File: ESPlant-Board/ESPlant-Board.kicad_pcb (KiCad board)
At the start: 2 copper layers, 22 x 127 mm, 35 parts, among them J1 Conn_01x05, U13 ESP32-C6-MINI-1/U, U3 Reset, U4 Boot, U5 Temp/Humid-Sensor, U6 Light sensor, U7 AMS1117-3_3, U8 MK-12C02-G025

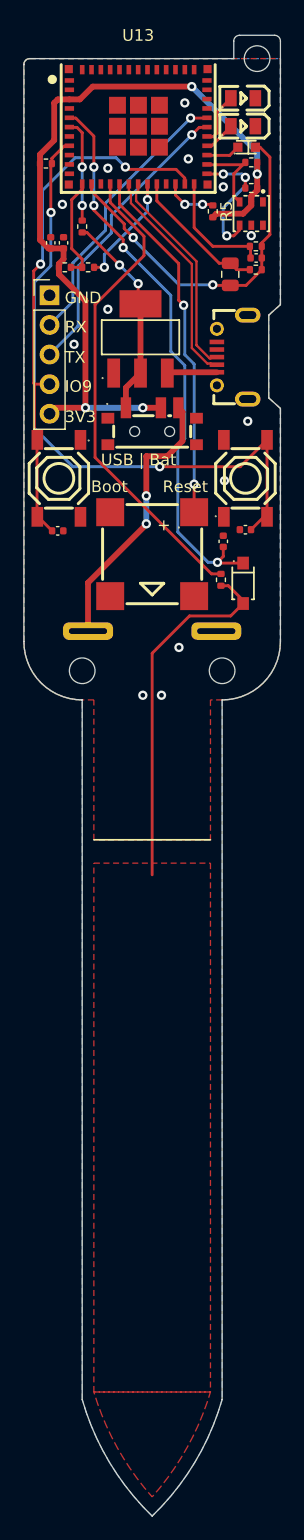
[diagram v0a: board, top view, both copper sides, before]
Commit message: Board: Replace Micro USB with USB type c
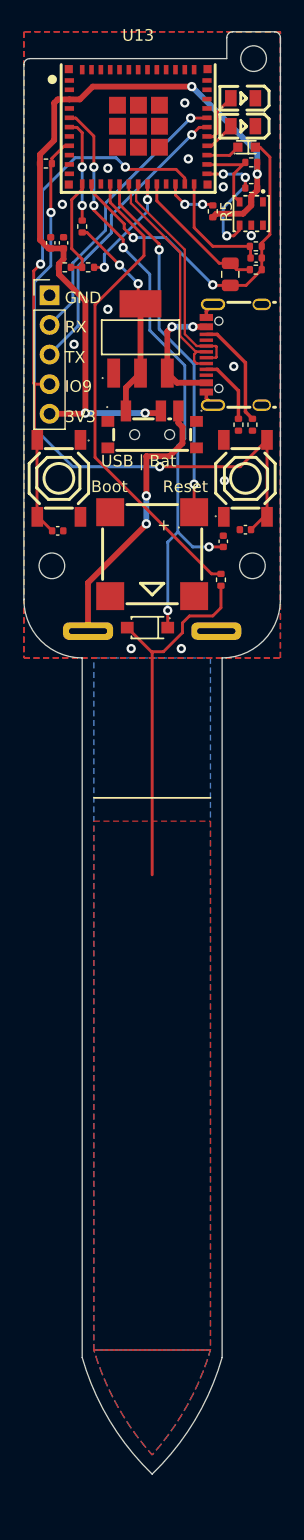
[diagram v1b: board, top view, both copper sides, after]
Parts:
- removed USB1: micro_USBFemale, CustomFootprints:MICRO-USB-SMD_5P-P0.65-H-F_C10418
- added R11: 5k1, Resistor_SMD:R_0402_1005Metric, F.Cu at (118.4, 131.4)
- added R12: 5k1, Resistor_SMD:R_0402_1005Metric, F.Cu at (119.6, 131.4)
- added U1: HC-TYPE-C-16P-01A-G, CustomFootprints:USB-C-SMD_G-SWITCH_GT-USB-7010EN, F.Cu at (118.0, 125.4)
- moved D2 9.04 mm to (110.6, 148.8), turned to 180 degrees
- moved U10 2.10 mm to (99.5, 143.5)
- moved U2 2.10 mm to (122.4, 143.5)
- moved U8 0.27 mm to (111.0, 131.8)
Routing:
- net Net-(U1-CC2): track 0.00 -> 9.42 mm
- net Net-(U7-VIN): track 4.28 -> 10.9 mm, vias 0 -> 2
- net Net-(U1-CC1): track 0.00 -> 5.92 mm
- net /AD_Capacitance: track 48.4 -> 53.2 mm, vias 4 -> 5
- net GND: track 0.04 -> 2.75 mm, vias 13 -> 12
- net /D-: track 19.0 -> 20.5 mm
- net /D+: track 18.3 -> 19.6 mm
- net /SensorCapV: track 31.4 -> 32.0 mm
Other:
- board size 22 x 127 mm -> 22 x 123.7 mm

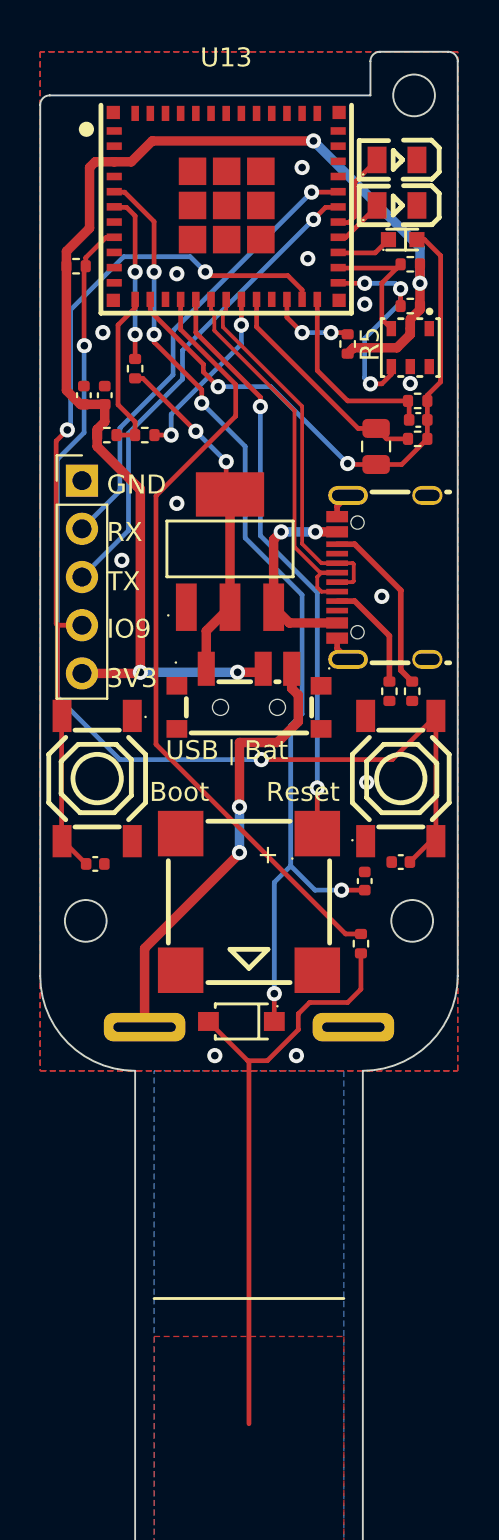
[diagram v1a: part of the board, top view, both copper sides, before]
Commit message: Board: Make board smaller
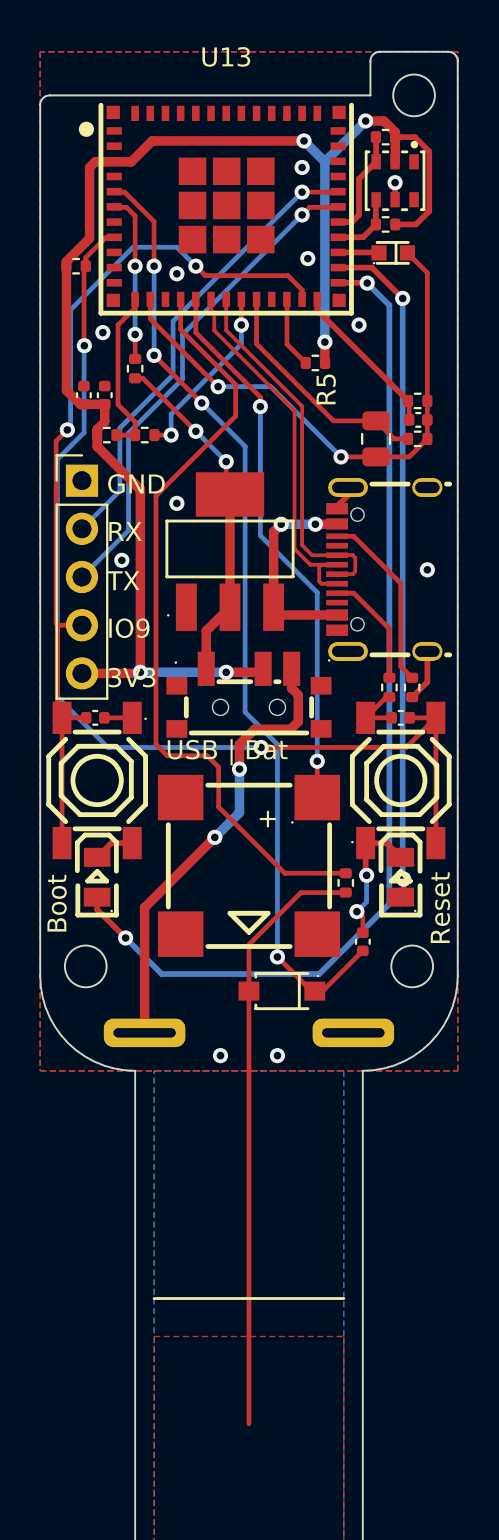
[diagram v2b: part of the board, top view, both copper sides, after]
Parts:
- moved D1 41.0 mm to (103.0, 141.2), turned to -90 degrees
- moved D3 35.4 mm to (119.0, 141.2), turned to -90 degrees
- moved U5 8.83 mm to (118.7, 104.5)
- moved C2 7.70 mm to (102.9, 132.8)
- moved C1 7.60 mm to (119.0, 132.8)
- moved R2 6.82 mm to (118.2, 102.2)
- moved R10 4.49 mm to (118.2, 106.8)
- moved R8 3.30 mm to (116.1, 141.5)
- moved C3 3.20 mm to (117.0, 144.6)
- moved D2 2.67 mm to (112.7, 147.2)
- moved R5 1.97 mm to (114.5, 114.1), turned to 0 degrees
- moved BZ1 1.90 mm to (111.0, 140.6)
- moved U6 0.86 mm to (118.6, 108.3)
- moved U1 0.42 mm to (118.0, 125.0)
- moved C7 0.40 mm to (117.7, 118.1)
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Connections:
- U13 pad 25: /TH_SDA -> /LED_GREEN
- U13 pad 26: /TH_SCL -> /LED_RED
- U13 pad 28: /LED_RED -> /TH_SDA
- U13 pad 29: /LED_GREEN -> /TH_SCL
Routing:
- net /LED_GREEN: track 4.47 -> 53.7 mm, vias 0 -> 2
- net /LED_RED: track 2.78 -> 35.7 mm, vias 0 -> 2
- net GND: track 2.75 -> 18.6 mm, vias 12 -> 13
- net /TH_SDA: track 12.0 -> 3.57 mm, vias 3 -> 0
- net +3V3: track 69.3 -> 77.3 mm, vias 4 -> 5
- net /AD_Capacitance: track 53.2 -> 50.3 mm, vias 5 -> 4
- net /Buzzer: track 30.8 -> 28.9 mm
- net /Light_Sensor_Select_1: track 10.2 -> 8.35 mm
- net /TH_SCL: track 7.38 -> 5.73 mm
- net /Light_Sensor_Analog: track 30.9 -> 29.2 mm
- net /Square_Wave_Signal: track 41.3 -> 40.4 mm
- net /EN: track 56.3 -> 55.4 mm
- net /Light_Sensor_In: track 2.94 -> 2.16 mm
- net /IO8: track 4.47 -> 3.71 mm, vias 2 -> 0
- net /Light_Sensor_Select_2: track 11.8 -> 12.4 mm
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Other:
- outline, holes or cut-outs redrawn

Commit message: Board: Add version number 2.1
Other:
- board text added: "ESPlant-v2.1"
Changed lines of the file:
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@@
     (effects (font (size 1 1) (thickness 0.15)) (justify left bottom mirror))
   )
-  (gr_text "M2" (at 121 102.5) (layer "B.SilkS")
+  (gr_text "M2" (at 120.9 102.8) (layer "B.SilkS")
     (effects (font (size 1 1) (thickness 0.15)) (justify left bottom mirror))
   )
@@
     (effects (font (size 1 1) (thickness 0.15)) (justify left bottom mirror))
   )
-  (gr_text "M2" (at 120.8 143.2) (layer "B.SilkS")
+  (gr_text "M2" (at 120.8 144.6) (layer "B.SilkS")
+    (effects (font (size 1 1) (thickness 0.15)) (justify left bottom mirror))
+  )
+  (gr_text "ESPlant-v2.1" (at 110.9 102.1) (layer "B.SilkS")
     (effects (font (size 1 1) (thickness 0.15)) (justify left bottom mirror))
   )
@@
     (effects (font (size 1 1) (thickness 0.15)) (justify left bottom mirror))
   )
-  (gr_text "M2" (at 103.6 143.2) (layer "B.SilkS")
+  (gr_text "M2" (at 103.6 144.6) (layer "B.SilkS")
     (effects (font (size 1 1) (thickness 0.15)) (justify left bottom mirror))
   )

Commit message: Board: Change from aht21 to aht21, fix kikit, produce board
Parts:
- U10, U11, U12, U2: footprint PCM_kikit:Tab_5mm -> CustomFootprints:MouseBites5mm
- moved U10 0.71 mm to (100.0, 143.0)
- moved U2 0.64 mm to (122.0, 143.0)
- moved U11 0.40 mm to (122.0, 104.0)
- moved U12 0.40 mm to (100.0, 104.0)
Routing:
- net GND: track 18.6 -> 19.9 mm, vias 13 -> 12
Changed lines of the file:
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@@
     )
   )
-  (footprint "PCM_kikit:Tab_5mm" (layer "F.Cu")
-    (at 122.45 104 180)
-    (descr "A symbol representing annotation for tab placement")
+  (footprint "CustomFootprints:MouseBites5mm" (layer "F.Cu")
+    (at 122.05 104 180)
     (property "Sheetfile" "ESPlant-Board.kicad_sch")
     (property "Sheetname" "")
     (property "dnp" "")
     (property "exclude_from_bom" "")
-    (attr exclude_from_pos_files exclude_from_bom)
-    (fp_text reference "U11" (at 0 -2) (layer "F.SilkS") hide
-        (effects (font (size 1 1) (thickness 0.15)))
-    )
-    (fp_text value "~" (at -2.75 -1) (layer "Dwgs.User")
-        (effects (font (size 1.2 1.2) (thickness 0.2)))
-    )
-    (fp_text user "KIKIT: width: 5mm" (at -5.5 0 90) (layer "Dwgs.User")
-        (effects (font (size 1 1) (thickness 0.15)))
-    )
-    (fp_line (start 0.25 0) (end -2.75 0)
+    (attr smd exclude_from_bom)
+    (fp_text reference "U11" (at 0 -0.5 180 unlocked) (layer "F.SilkS") hide
+        (effects (font (size 1 1) (thickness 0.1)))
+    )
+    (fp_text value "~" (at 0 1 180 unlocked) (layer "F.Fab")
+        (effects (font (size 1 1) (thickness 0.15)))
+    )
+    (fp_text user "KIKIT: width: 5mm" (at -6.004 -0.04 270) (layer "Dwgs.User")
+        (effects (font (size 1 1) (thickness 0.15)))
+    )
+    (fp_text user "${REFERENCE}" (at 0 2.5 180 unlocked) (layer "F.Fab")
+        (effects (font (size 1 1) (thickness 0.15)))
+    )
+    (fp_line (start -0.254 -0.04) (end -3.254 -0.04)
       (stroke (width 0.3) (type solid)) (layer "Dwgs.User"))
-    (fp_line (start 0.25 0) (end -0.75 -1)
+    (fp_line (start -0.254 -0.04) (end -1.254 -1.04)
       (stroke (width 0.3) (type solid)) (layer "Dwgs.User"))
-    (fp_line (start 0.25 0) (end -0.75 1)
+    (fp_line (start -0.254 -0.04) (end -1.254 0.96)
       (stroke (width 0.3) (type solid)) (layer "Dwgs.User"))
-    (fp_line (start 0.25 2.5) (end 0.25 -2.5)
+    (fp_line (start -0.254 2.46) (end -0.254 -2.54)
       (stroke (width 0.3) (type solid)) (layer "Dwgs.User"))
   )
-  (footprint "PCM_kikit:Tab_5mm" (layer "F.Cu")
-    (at 99.6 104)
-    (descr "A symbol representing annotation for tab placement")
+  (footprint "CustomFootprints:MouseBites5mm" (layer "F.Cu")
+    (at 100 104)
     (property "Sheetfile" "ESPlant-Board.kicad_sch")
     (property "Sheetname" "")
     (property "dnp" "")
     (property "exclude_from_bom" "")
-    (attr exclude_from_pos_files exclude_from_bom)
-    (fp_text reference "U12" (at 0 -2) (layer "F.SilkS") hide
-        (effects (font (size 1 1) (thickness 0.15)))
-    )
-    (fp_text value "~" (at -2.75 -1) (layer "Dwgs.User")
-        (effects (font (size 1.2 1.2) (thickness 0.2)))
-    )
-    (fp_text user "KIKIT: width: 5mm" (at -5.5 0 90) (layer "Dwgs.User")
-        (effects (font (size 1 1) (thickness 0.15)))
-    )
-    (fp_line (start 0.25 0) (end -2.75 0)
+    (attr smd exclude_from_bom)
+    (fp_text reference "U12" (at 0 -0.5 unlocked) (layer "F.SilkS") hide
+        (effects (font (size 1 1) (thickness 0.1)))
+    )
+    (fp_text value "~" (at 0 1 unlocked) (layer "F.Fab")
+        (effects (font (size 1 1) (thickness 0.15)))
+    )
+    (fp_text user "KIKIT: width: 5mm" (at -6.004 -0.04 90) (layer "Dwgs.User")
+        (effects (font (size 1 1) (thickness 0.15)))
+    )
+    (fp_text user "${REFERENCE}" (at 0 2.5 unlocked) (layer "F.Fab")
+        (effects (font (size 1 1) (thickness 0.15)))
+    )
+    (fp_line (start -0.254 -0.04) (end -3.254 -0.04)
       (stroke (width 0.3) (type solid)) (layer "Dwgs.User"))
-    (fp_line (start 0.25 0) (end -0.75 -1)
+    (fp_line (start -0.254 -0.04) (end -1.254 -1.04)
       (stroke (width 0.3) (type solid)) (layer "Dwgs.User"))
-    (fp_line (start 0.25 0) (end -0.75 1)
+    (fp_line (start -0.254 -0.04) (end -1.254 0.96)
       (stroke (width 0.3) (type solid)) (layer "Dwgs.User"))
-    (fp_line (start 0.25 2.5) (end 0.25 -2.5)
+    (fp_line (start -0.254 2.46) (end -0.254 -2.54)
       (stroke (width 0.3) (type solid)) (layer "Dwgs.User"))
   )
@@
     (tags "SENSOR-SMD_L3.0-W3.0-P1.00-BR footprint C2827328")
     (property "JLCPCB Position Offset" "")
-    (property "LCSC" "C2827328")
-    (property "MPN" "C2827328")
+    (property "LCSC" "C2757850")
+    (property "MPN" "C2757850")
     (property "Sheetfile" "ESPlant-Board.kicad_sch")
     (property "Sheetname" "")
@@
     )
   )
-  (footprint "PCM_kikit:Tab_5mm" (layer "F.Cu")
-    (at 99.5 143.5)
-    (descr "A symbol representing annotation for tab placement")
+  (footprint "CustomFootprints:MouseBites5mm" (layer "F.Cu")
+    (at 100 143)
     (property "Sheetfile" "ESPlant-Board.kicad_sch")
     (property "Sheetname" "")
     (property "dnp" "")
     (property "exclude_from_bom" "")
-    (attr exclude_from_pos_files exclude_from_bom)
-    (fp_text reference "U10" (at 0 -2) (layer "F.SilkS") hide
-        (effects (font (size 1 1) (thickness 0.15)))
-    )
-    (fp_text value "~" (at -2.75 -1) (layer "Dwgs.User")
-        (effects (font (size 1.2 1.2) (thickness 0.2)))
-    )
-    (fp_text user "KIKIT: width: 5mm" (at -5.5 0 90) (layer "Dwgs.User")
-        (effects (font (size 1 1) (thickness 0.15)))
-    )
-    (fp_line (start 0.25 0) (end -2.75 0)
+    (attr smd exclude_from_bom)
+    (fp_text reference "U10" (at 0 -0.5 unlocked) (layer "F.SilkS") hide
+        (effects (font (size 1 1) (thickness 0.1)))
+    )
+    (fp_text value "~" (at 0 1 unlocked) (layer "F.Fab")
+        (effects (font (size 1 1) (thickness 0.15)))
+    )
+    (fp_text user "KIKIT: width: 5mm" (at -6.004 -0.04 90) (layer "Dwgs.User")
+        (effects (font (size 1 1) (thickness 0.15)))
+    )
+    (fp_text user "${REFERENCE}" (at 0 2.5 unlocked) (layer "F.Fab")
+        (effects (font (size 1 1) (thickness 0.15)))
+    )
+    (fp_line (start -0.254 -0.04) (end -3.254 -0.04)
       (stroke (width 0.3) (type solid)) (layer "Dwgs.User"))
-    (fp_line (start 0.25 0) (end -0.75 -1)
+    (fp_line (start -0.254 -0.04) (end -1.254 -1.04)
       (stroke (width 0.3) (type solid)) (layer "Dwgs.User"))
-    (fp_line (start 0.25 0) (end -0.75 1)
+    (fp_line (start -0.254 -0.04) (end -1.254 0.96)
       (stroke (width 0.3) (type solid)) (layer "Dwgs.User"))
-    (fp_line (start 0.25 2.5) (end 0.25 -2.5)
+    (fp_line (start -0.254 2.46) (end -0.254 -2.54)
       (stroke (width 0.3) (type solid)) (layer "Dwgs.User"))
   )
@@
     )
   )
-  (footprint "PCM_kikit:Tab_5mm" (layer "F.Cu")
-    (at 122.4 143.5 180)
-    (descr "A symbol representing annotation for tab placement")
+  (footprint "CustomFootprints:MouseBites5mm" (layer "F.Cu")
+    (at 122 143 180)
     (property "Sheetfile" "ESPlant-Board.kicad_sch")
     (property "Sheetname" "")
     (property "dnp" "")
     (property "exclude_from_bom" "")
-    (attr exclude_from_pos_files exclude_from_bom)
-    (fp_text reference "U2" (at 0 -2) (layer "F.SilkS") hide
-        (effects (font (size 1 1) (thickness 0.15)))
-    )
-    (fp_text value "~" (at -2.75 -1) (layer "Dwgs.User")
-        (effects (font (size 1.2 1.2) (thickness 0.2)))
-    )
-    (fp_text user "KIKIT: width: 5mm" (at -5.5 0 90) (layer "Dwgs.User")
-        (effects (font (size 1 1) (thickness 0.15)))
-    )
-    (fp_line (start 0.25 0) (end -2.75 0)
+    (attr smd exclude_from_bom)
+    (fp_text reference "U2" (at 0 -0.5 180 unlocked) (layer "F.SilkS") hide
+        (effects (font (size 1 1) (thickness 0.1)))
+    )
+    (fp_text value "~" (at 0 1 180 unlocked) (layer "F.Fab")
+        (effects (font (size 1 1) (thickness 0.15)))
+    )
+    (fp_text user "KIKIT: width: 5mm" (at -6.004 -0.04 270) (layer "Dwgs.User")
+        (effects (font (size 1 1) (thickness 0.15)))
+    )
+    (fp_text user "${REFERENCE}" (at 0 2.5 180 unlocked) (layer "F.Fab")
+        (effects (font (size 1 1) (thickness 0.15)))
+    )
+    (fp_line (start -0.254 -0.04) (end -3.254 -0.04)
       (stroke (width 0.3) (type solid)) (layer "Dwgs.User"))
-    (fp_line (start 0.25 0) (end -0.75 -1)
+    (fp_line (start -0.254 -0.04) (end -1.254 -1.04)
       (stroke (width 0.3) (type solid)) (layer "Dwgs.User"))
-    (fp_line (start 0.25 0) (end -0.75 1)
+    (fp_line (start -0.254 -0.04) (end -1.254 0.96)
       (stroke (width 0.3) (type solid)) (layer "Dwgs.User"))
-    (fp_line (start 0.25 2.5) (end 0.25 -2.5)
+    (fp_line (start -0.254 2.46) (end -0.254 -2.54)
       (stroke (width 0.3) (type solid)) (layer "Dwgs.User"))
   )
@@
   (segment (start 118.239809 131.71) (end 117.149784 132.800025) (width 0.25) (layer "F.Cu") (net 7))
   (segment (start 120.4 130.91) (end 120.4 129.302063) (width 0.3) (layer "F.Cu") (net 7))
+  (segment (start 115.644856 128.727006) (end 115.644856 128.18192) (width 0.25) (layer "F.Cu") (net 7))
   (segment (start 119.6 131.71) (end 120.4 130.91) (width 0.3) (layer "F.Cu") (net 7))
   (segment (start 118.4 131.71) (end 118.239809 131.71) (width 0.25) (layer "F.Cu") (net 7))
@@
   (segment (start 115.644856 121.782124) (end 115.644856 121.655016) (width 0.3) (layer "F.Cu") (net 7))
   (segment (start 103.38 132.8) (end 104.850166 132.8) (width 0.25) (layer "F.Cu") (net 7))
+  (segment (start 116.219913 129.302063) (end 115.644856 128.727006) (width 0.25) (layer "F.Cu") (net 7))
   (segment (start 103.749733 139.399975) (end 103 140.149708) (width 0.3) (layer "F.Cu") (net 7))
   (segment (start 117.149809 132.8) (end 117.149784 132.800025) (width 0.25) (layer "F.Cu") (net 7))
@@
   (via (at 103.3 112.5) (size 0.8) (drill 0.4) (layers "F.Cu" "B.Cu") (free) (net 7))
   (via (at 118.7 104.6) (size 0.8) (drill 0.4) (layers "F.Cu" "B.Cu") (net 7))
-  (via (at 107.2 109.4) (size 0.8) (drill 0.4) (layers "F.Cu" "B.Cu") (net 7))
   (via (at 114.1 108.6) (size 0.8) (drill 0.4) (layers "F.Cu" "B.Cu") (free) (net 7))
   (segment (start 116.687701 143.012299) (end 117.2 142.5) (width 0.25) (layer "B.Cu") (net 7))
